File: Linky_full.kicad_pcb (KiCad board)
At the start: 2 copper layers, 100 x 70 mm, 59 parts, among them J23 USB_C_Receptacle_USB2.0_16P, J3 Linky, Q2 AO3400A, Q7 UMH3N, SW3 SW_SPST, SW5 SW_SPST, U13 USBLC6-2P6, U2 LM2575-5.0BU, U24 CP2104, U3 TLV1117LV-3.3, U4 LTV-814, U7 ESP32-S3-WROOM-1

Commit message: Placa ruteada y con GND
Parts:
- removed C40: 4u7, Capacitor_SMD:C_0805_2012Metric_Pad1.18x1.45mm_HandSolder
- moved FB4 201.9 mm to (76.5, 93.2)
- moved Q2 197.8 mm to (75.6, 85.7)
- moved J23 196.2 mm to (66.5, 98.9), turned to -90 degrees
- moved F4 195.2 mm to (82.7, 93.5)
- moved U4 191.8 mm to (70.1, 77.7), turned to -90 degrees
- moved U13 190.6 mm to (85.9, 99.0)
- moved C37 185.9 mm to (87.5, 89.7)
- moved U24 173.5 mm to (98.3, 99.3), turned to 180 degrees
- moved C41 166.1 mm to (104.5, 82.3)
- moved C39 162.1 mm to (94.6, 88.8)
- moved R84 160.7 mm to (74.8, 97.8)
- moved R6 155.7 mm to (64.8, 78.3), turned to -90 degrees
- moved Q7 155.7 mm to (125.9, 97.6)
- moved R32 155.7 mm to (74.8, 101.5)
- moved R8 150.2 mm to (75.4, 88.6), turned to 180 degrees
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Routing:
- net +3.3V: track 0.00 -> 207.8 mm, vias 0 -> 3
- net GND: track 3.95 -> 134.2 mm, vias 0 -> 5
- net Signal: track 0.00 -> 93.7 mm, vias 0 -> 2
- net /RST: track 0.00 -> 82.4 mm
- net +5V: track 47.8 -> 114.4 mm, vias 0 -> 2
- net /Boot: track 0.00 -> 60.9 mm, vias 0 -> 2
- net /RX: track 0.00 -> 50.6 mm
- net /TX: track 0.00 -> 50.2 mm
- net VDD_SPI: track 0.00 -> 40.7 mm
- net /RTS: track 0.00 -> 34.9 mm
- net /DTR: track 0.00 -> 30.8 mm, vias 0 -> 2
- net Net-(U24-D-): track 0.00 -> 28.4 mm, vias 0 -> 2
- net Net-(U24-D+): track 0.00 -> 27.8 mm, vias 0 -> 2
- net Net-(U24-RXD): track 0.00 -> 20.4 mm
- net Net-(J23-D+-PadA6): track 0.00 -> 17.1 mm
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- added copper zone on F.Cu, net GND

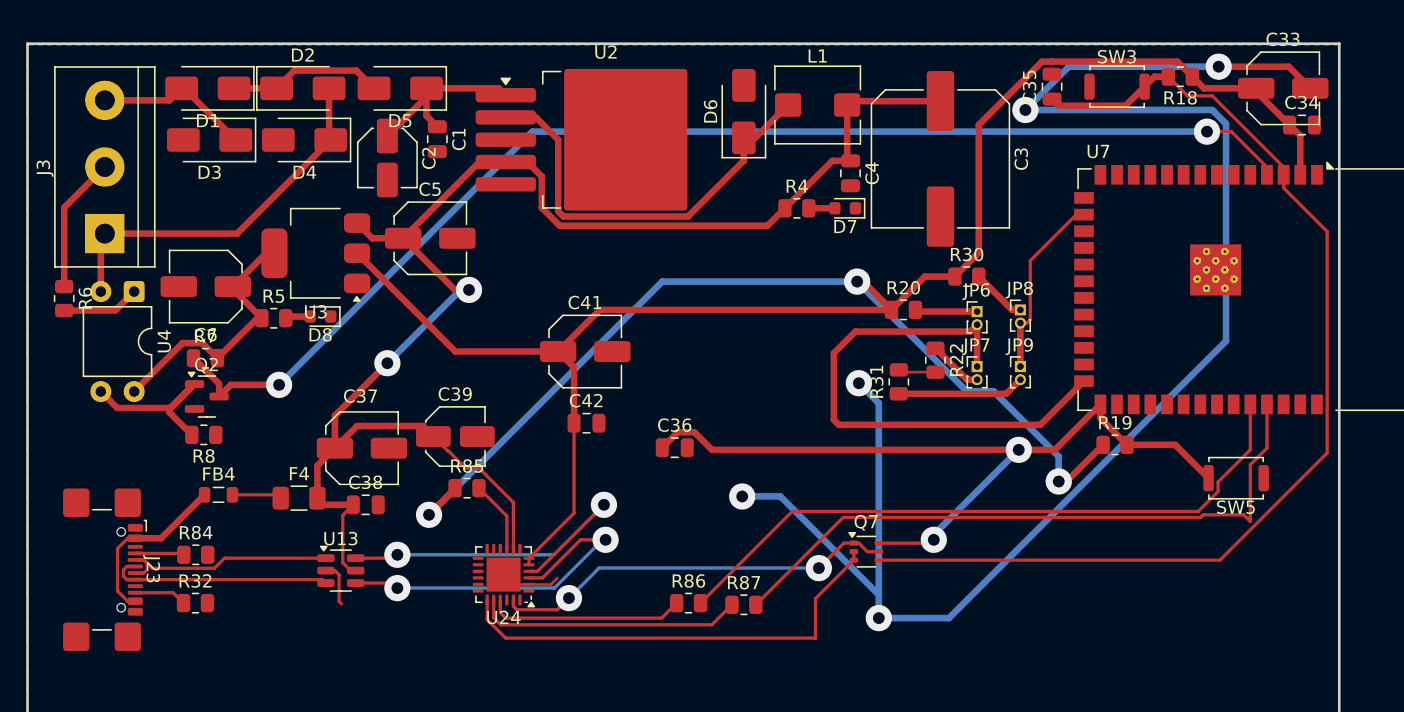
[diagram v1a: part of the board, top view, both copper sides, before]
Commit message: Versión funcional con esquema completo, pcb y enrutado completo de pistas. Falta mejorar la posición y el tamaño de la pcb
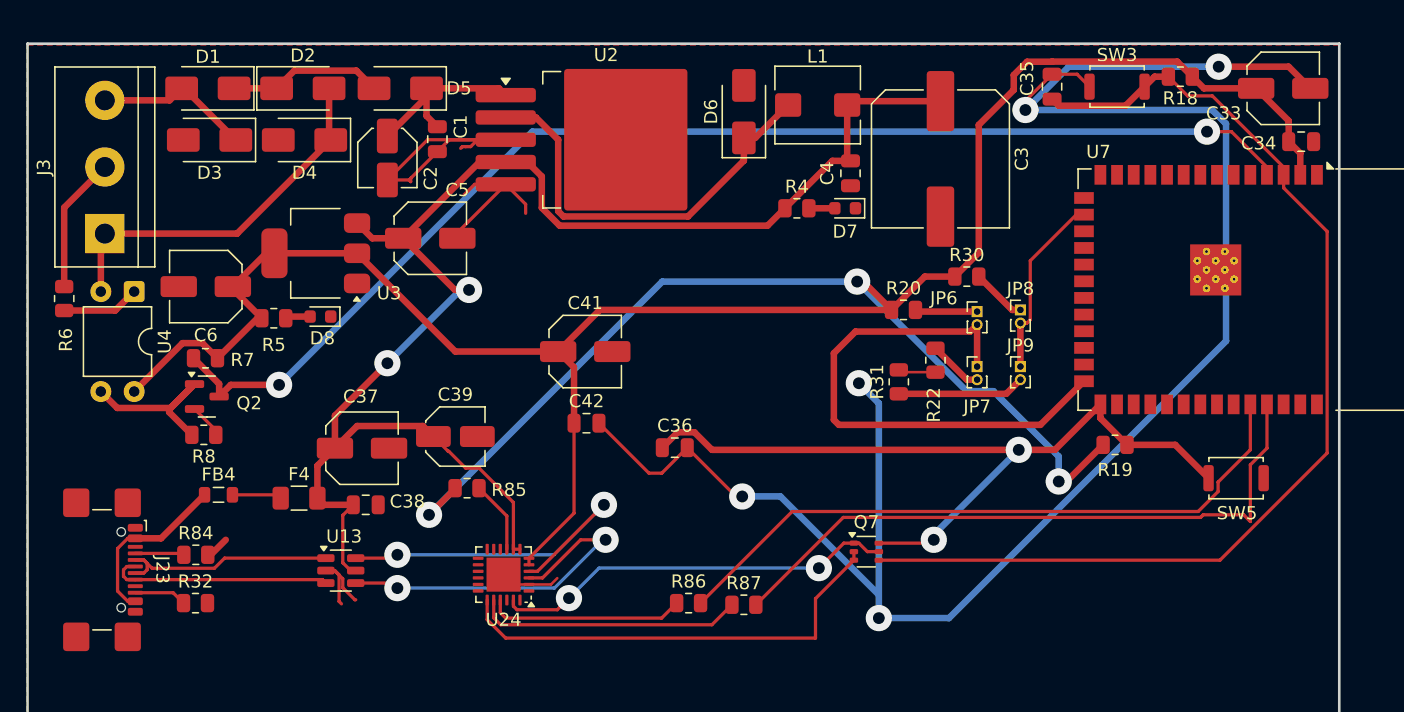
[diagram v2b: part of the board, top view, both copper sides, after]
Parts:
- moved C34 1.27 mm to (159.1, 66.3)
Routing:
- net GND: track 134.2 -> 200.5 mm
- net +3.3V: track 207.8 -> 215.0 mm
- net +5V: track 114.4 -> 114.9 mm

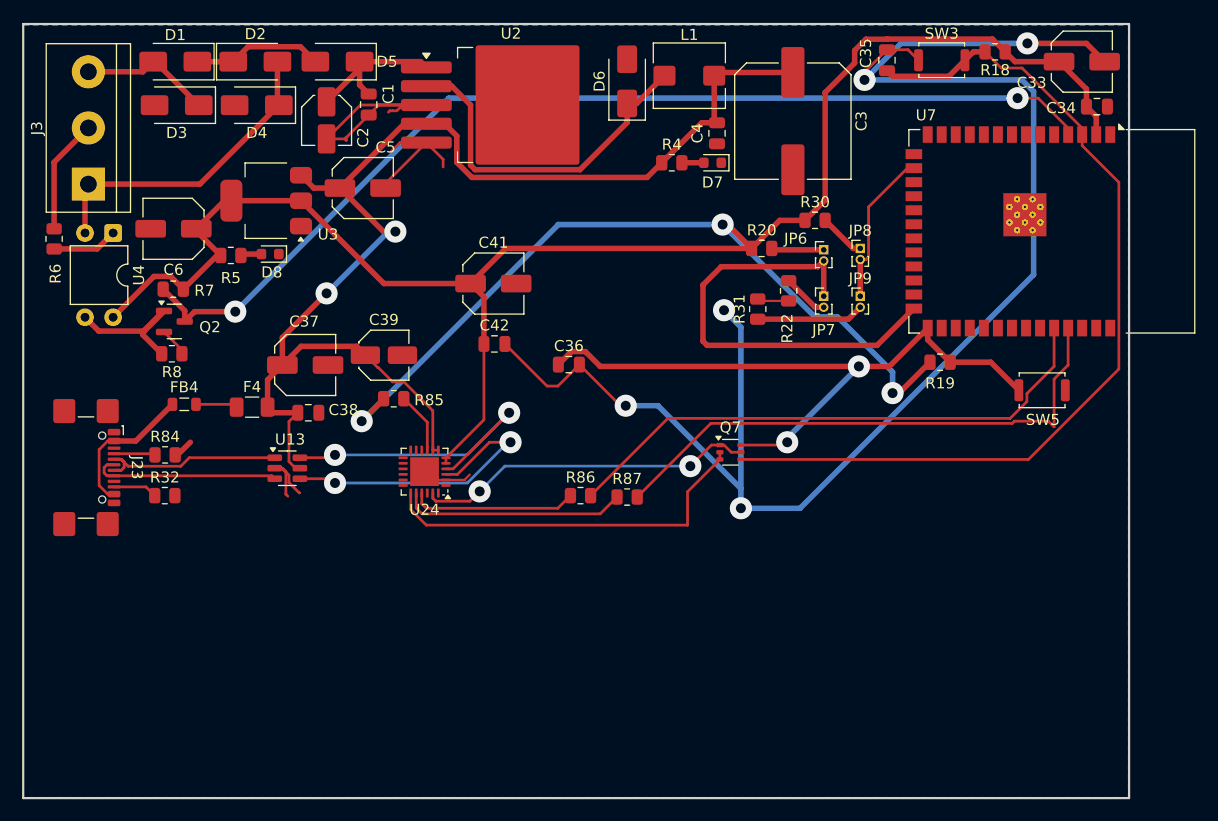
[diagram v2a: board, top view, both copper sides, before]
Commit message: Versión compacta y ruteada terminada. Falta el silkscreen y verificar DRC
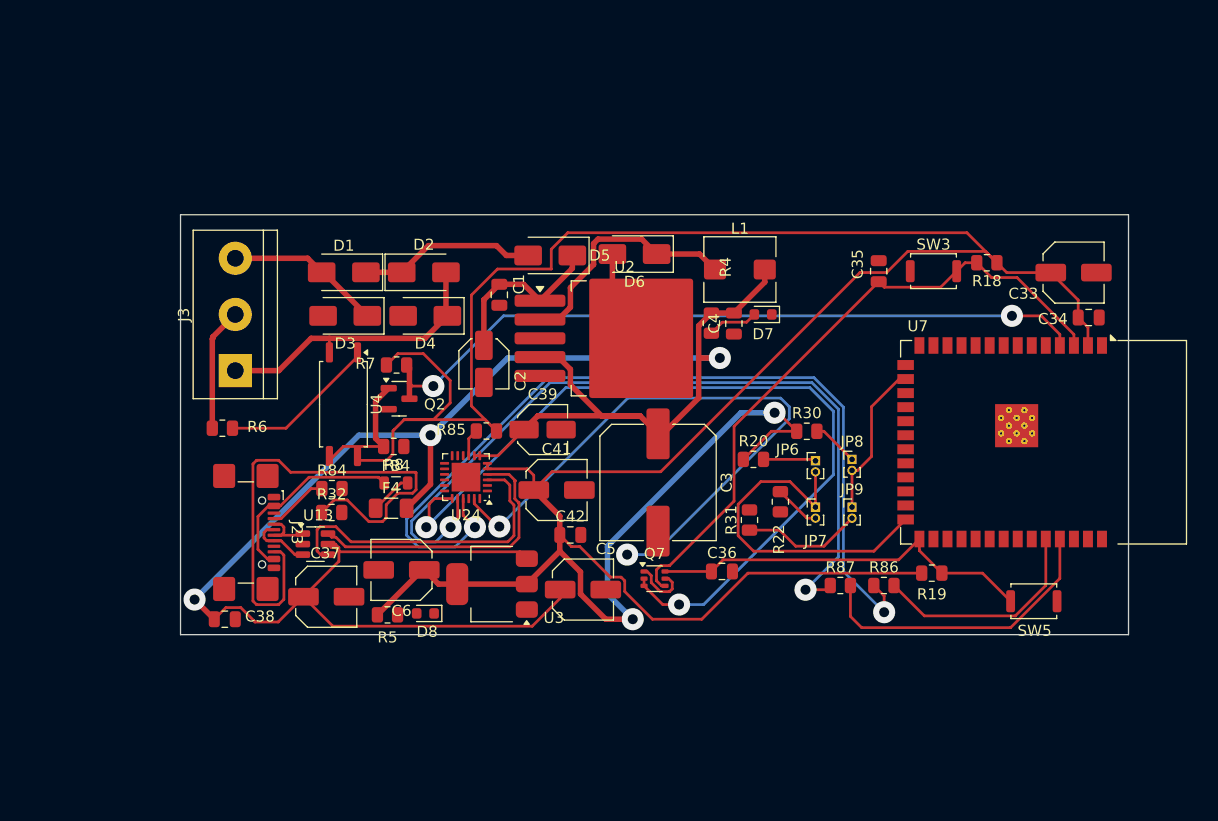
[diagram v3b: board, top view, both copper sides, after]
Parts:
- U4: value LTV-814 -> EL817C; footprint Package_DIP:DIP-4_W7.62mm -> Package_SO:SOP-4_7.5x4.1mm_P2.54mm
- moved C5 41.4 mm to (112.6, 110.0)
- moved U3 40.2 mm to (104.4, 109.5)
- moved C6 37.1 mm to (96.2, 108.2)
- moved R5 35.5 mm to (94.9, 112.3)
- moved D8 35.4 mm to (98.3, 112.1)
- moved C3 34.9 mm to (119.4, 100.3)
- moved R86 28.6 mm to (139.8, 109.6)
- moved C2 26.2 mm to (103.6, 89.6)
- moved D5 26.0 mm to (109.6, 79.8)
- moved U4 26.0 mm to (90.9, 93.2)
- moved D2 24.4 mm to (98.2, 81.3)
- moved D1 24.4 mm to (91.0, 81.3)
- moved D3 24.4 mm to (91.1, 85.2)
- moved D4 24.4 mm to (98.3, 85.2)
- moved U2 23.5 mm to (116.4, 87.2)
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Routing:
- net GND: track 200.5 -> 8.70 mm, vias 5 -> 0
- net +5V: track 114.9 -> 181.3 mm, vias 2 -> 3
- net Net-(U24-TXD): track 15.1 -> 80.6 mm, vias 0 -> 2
- net +3.3V: track 215.0 -> 276.9 mm, vias 3 -> 2
- net Net-(U24-RXD): track 20.4 -> 73.1 mm, vias 0 -> 2
- net Net-(J23-CC2): track 4.00 -> 49.2 mm
- net /RTS: track 34.9 -> 76.6 mm, vias 0 -> 2
- net /RX: track 50.6 -> 20.2 mm
- net /DTR: track 30.8 -> 60.9 mm
- net Signal: track 93.7 -> 66.4 mm
- net /Boot: track 60.9 -> 35.4 mm, vias 2 -> 0
- net /RST: track 82.4 -> 59.3 mm
- net /TX: track 50.2 -> 27.6 mm
- net Net-(J23-D--PadA7): track 17.0 -> 5.17 mm
- net Net-(J23-D+-PadA6): track 17.1 -> 5.63 mm
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- removed copper zone on F.Cu, net GND
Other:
- board size 100 x 70 mm -> 85.7 x 38 mm

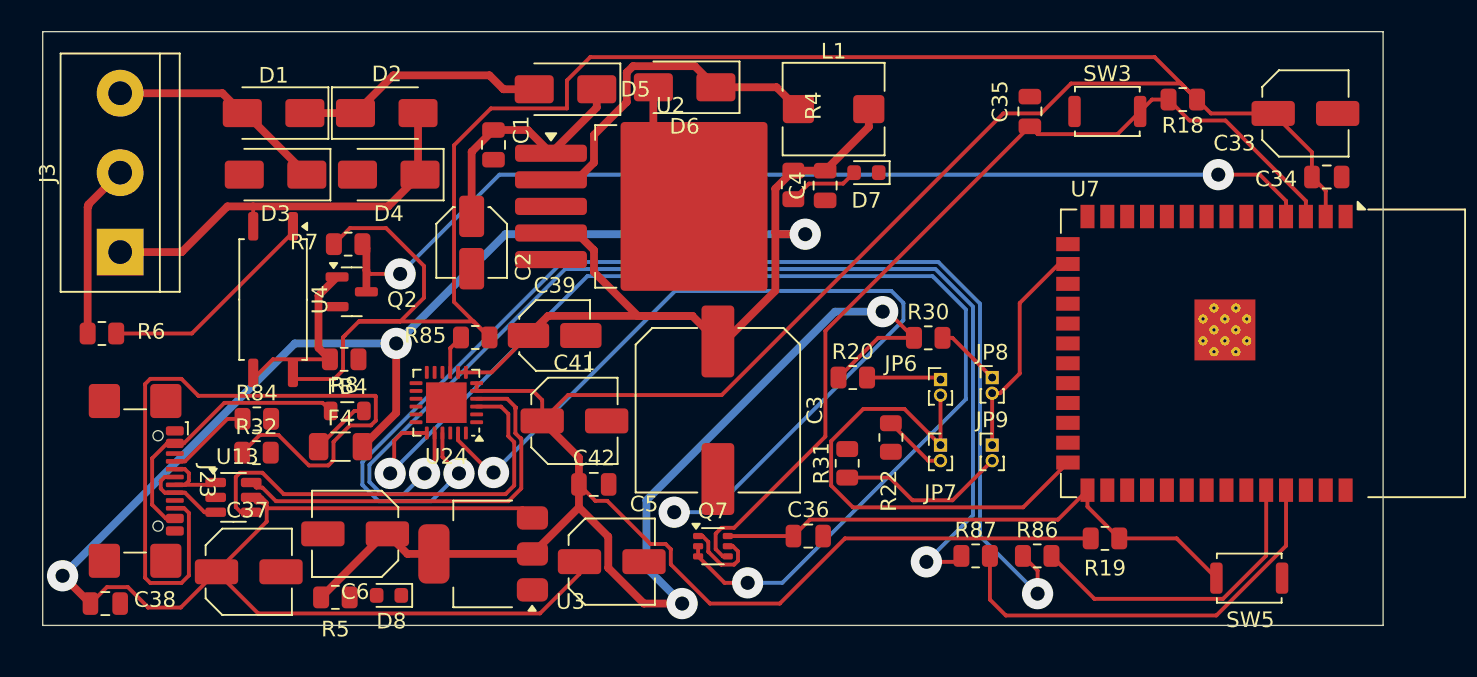
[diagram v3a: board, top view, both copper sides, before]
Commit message: Silkscreen terminado y versión mecanizable
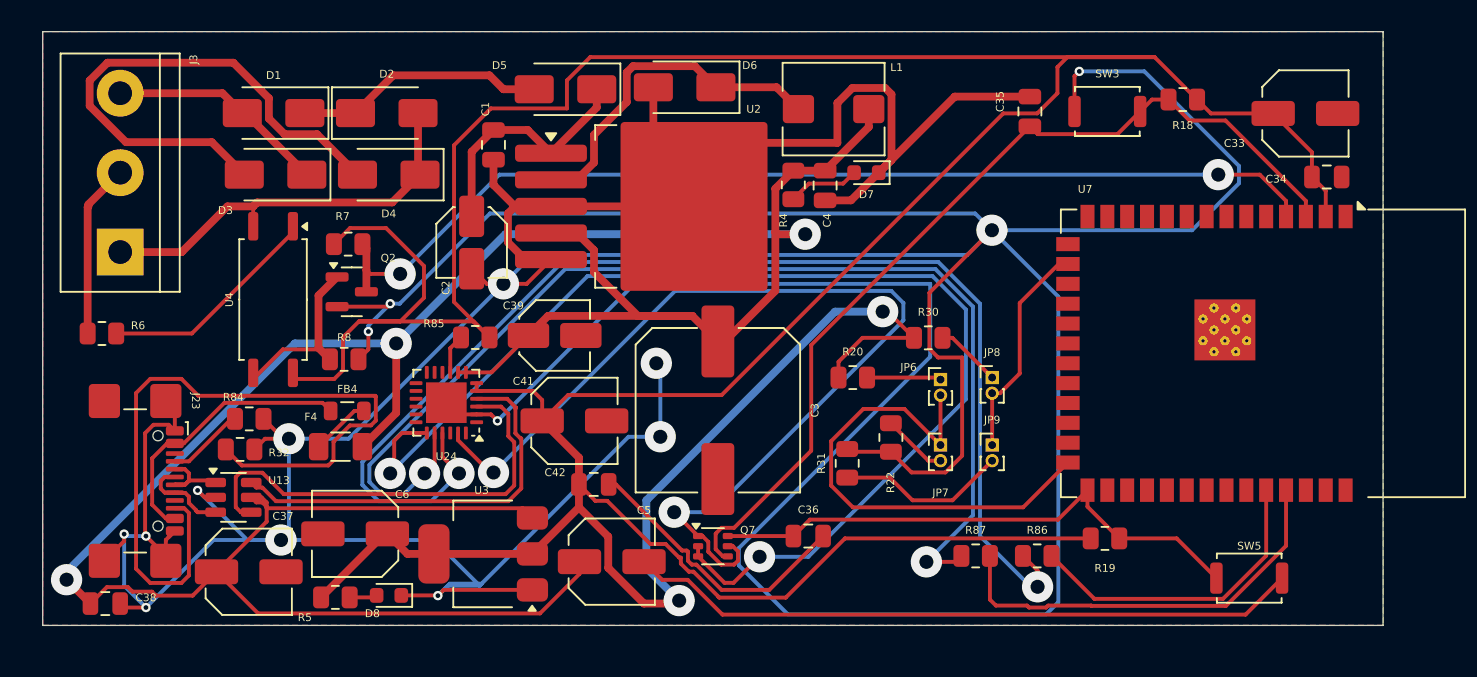
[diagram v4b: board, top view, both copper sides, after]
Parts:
- moved R32 1.07 mm to (88.8, 102.8)
- moved R84 0.48 mm to (89.4, 100.8)
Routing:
- net GND: track 8.70 -> 540.6 mm, vias 0 -> 15
- net /DTR: track 60.9 -> 63.1 mm
- net +3.3V: track 276.9 -> 275.0 mm
- net Net-(D8-A): track 0.00 -> 1.78 mm
- net +5V: track 181.3 -> 180.4 mm
- net Net-(J23-CC2): track 49.2 -> 49.8 mm
- net Net-(U24-TXD): track 80.6 -> 80.0 mm
- net Net-(Q2-G): track 11.5 -> 12.0 mm
- added copper zone on F.Cu, net GND
